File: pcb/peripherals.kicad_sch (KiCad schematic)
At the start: 34 parts, among them Q8 AO3407A, Q9 BSS138, SW4 GENERAL, SW5 GENERAL, SW6 GENERAL, SW7 GENERAL, SW8 SW_DIP_x04, U14 CAT24C32YI-GT3, U15 PCF8563T, U16 PCA9555PW, Y2 32.768kHz 9pF

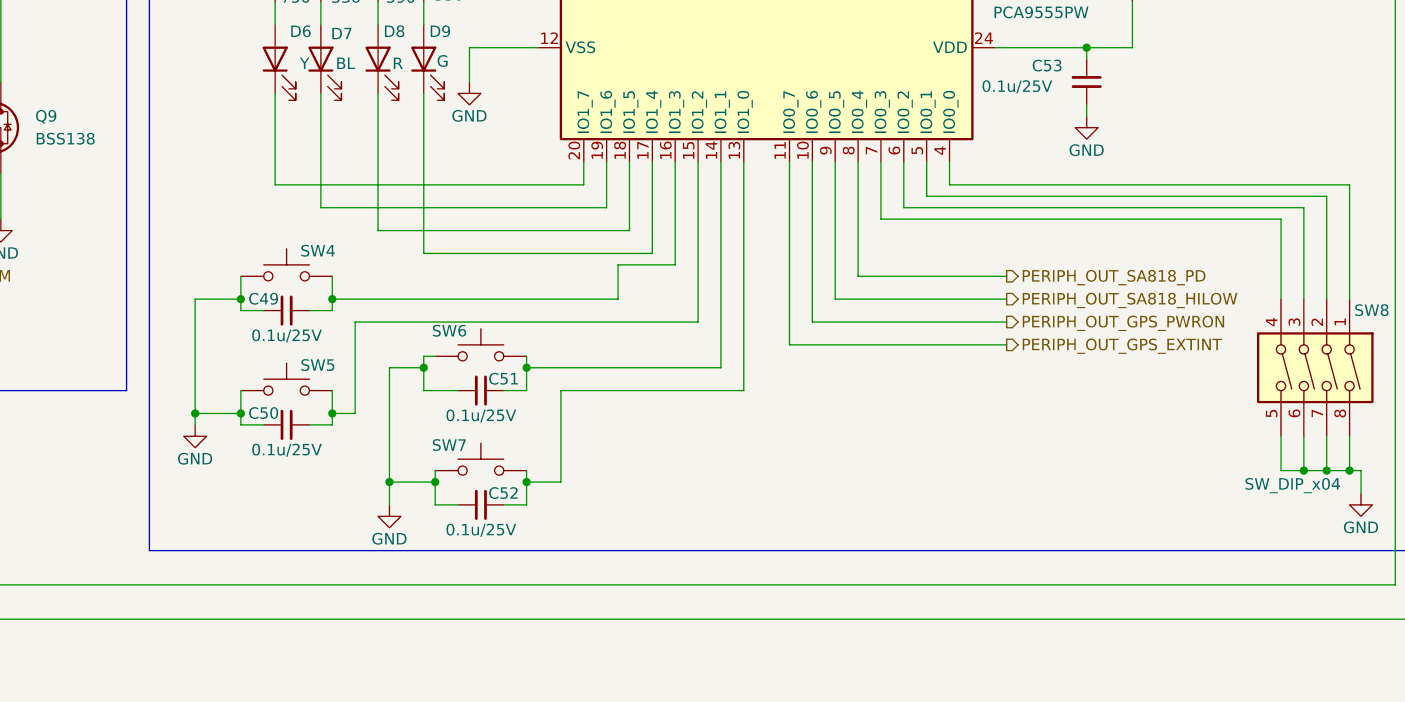
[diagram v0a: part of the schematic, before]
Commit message: audio path
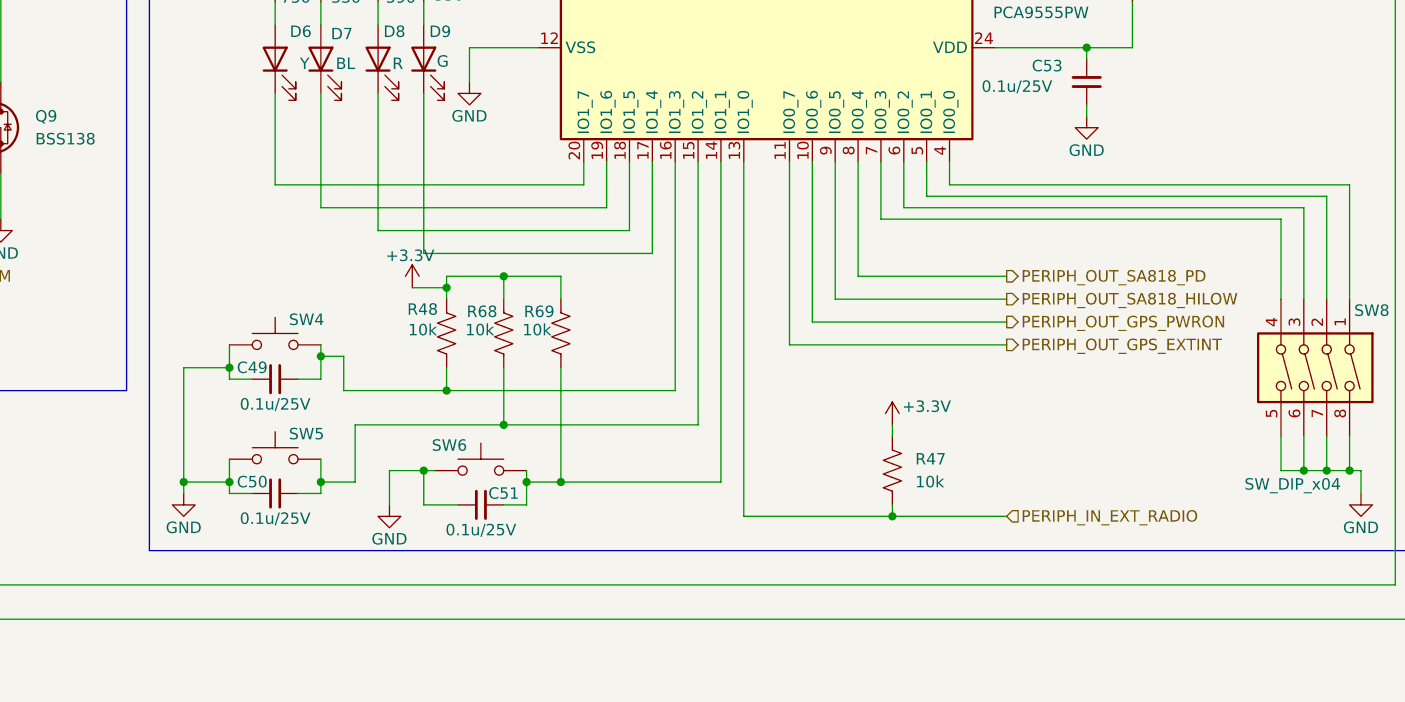
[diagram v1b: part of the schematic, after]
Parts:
- removed C52: 0.1u/25V, Capacitor_SMD:C_0603_1608Metric, symbol Device:C_Small
- removed SW7: GENERAL, Button_Switch_SMD:SW_SPST_PTS645Sx43SMTR92, symbol Switch:SW_Push
- added R47, R48, R68, R69: 10k, Resistor_SMD:R_0603_1608Metric, symbol Device:R_US
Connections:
- net +3.3V: now also R47.2, R48.1, R68.1, R69.1
- net PERIPH_IN_EXT_RADIO: now reaches U16.13 (IO1_0)
- net PERIPH_IN_EXT_RADIO: now also R47.1
- net at C50.2, SW5.1, U16.15 (IO1_2): now also R68.2
- net at C51.1, SW6.2, U16.14 (IO1_1): now also R69.2
- net at C49.2, SW4.1, U16.16 (IO1_3): now also R48.2
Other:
- moved on the sheet: C49, C50, C51, SW4, SW5, SW6

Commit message: annotations
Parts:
- removed R47: 10k, Resistor_SMD:R_0603_1608Metric, symbol Device:R_US
- added C52: 0.1u/25V, Capacitor_SMD:C_0603_1608Metric, symbol Device:C_Small
- added J6: Conn_01x03, Connector_JST:JST_PH_B3B-PH-SM4-TB_1x03-1MP_P2.00mm_Vertical, symbol Connector_Generic:Conn_01x03
- added JP26: GND IO0_7, Jumper:SolderJumper-2_P1.3mm_Open_TrianglePad1.0x1.5mm, symbol Jumper:SolderJumper_2_Open
- added R70, R71: 10k, Resistor_SMD:R_0603_1608Metric, symbol Device:R_US
- added SW7: GENERAL, Button_Switch_SMD:SW_SPST_PTS645Sx43SMTR92, symbol Switch:SW_Push
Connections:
- net +3.3V: now also R70.1, R71.1; no longer Q8.2 (S)
- net GND: now also C52.2, J6.3 (Pin_3), JP26.2 (B), SW7.1
- net at C47.1, D4.3, D5.3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: now also Q8.2 (S)
- net PERIPH_IN_EXT_RADIO: no longer names the net of U16.13 (IO1_0)
- net PERIPH_IN_EXT_RADIO: now also C52.1, R70.2, SW7.2
- net PERIPH_OUT_GPS_EXTINT: no longer names the net of U16.11 (IO0_7)
- net PERIPH_OUT_GPS_EXTINT: now also J6.2 (Pin_2), JP26.1 (A)
- new net: J6.1 (Pin_1), R71.2
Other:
- note added: "** If in deep sleep: wake up Q1 main power switch"
- note added: "**Extra IO"
- note added: "**If running normally: INT to MCU"
- note added: "**LED Indicators"
- note added: "BATTERY BACKUP"
- note added: "PERIPHERALS"
- moved on the sheet: BT3, D5, Q9, R35, R36
